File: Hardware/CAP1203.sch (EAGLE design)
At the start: 25 parts, among them J1 Qwiic Right Angle, J2 Qwiic Right Angle, J3 Cap Touch Breakout Pins, J4 I2C Breakout Pins, U1 Cap Touch Slider, U2 CAP1203

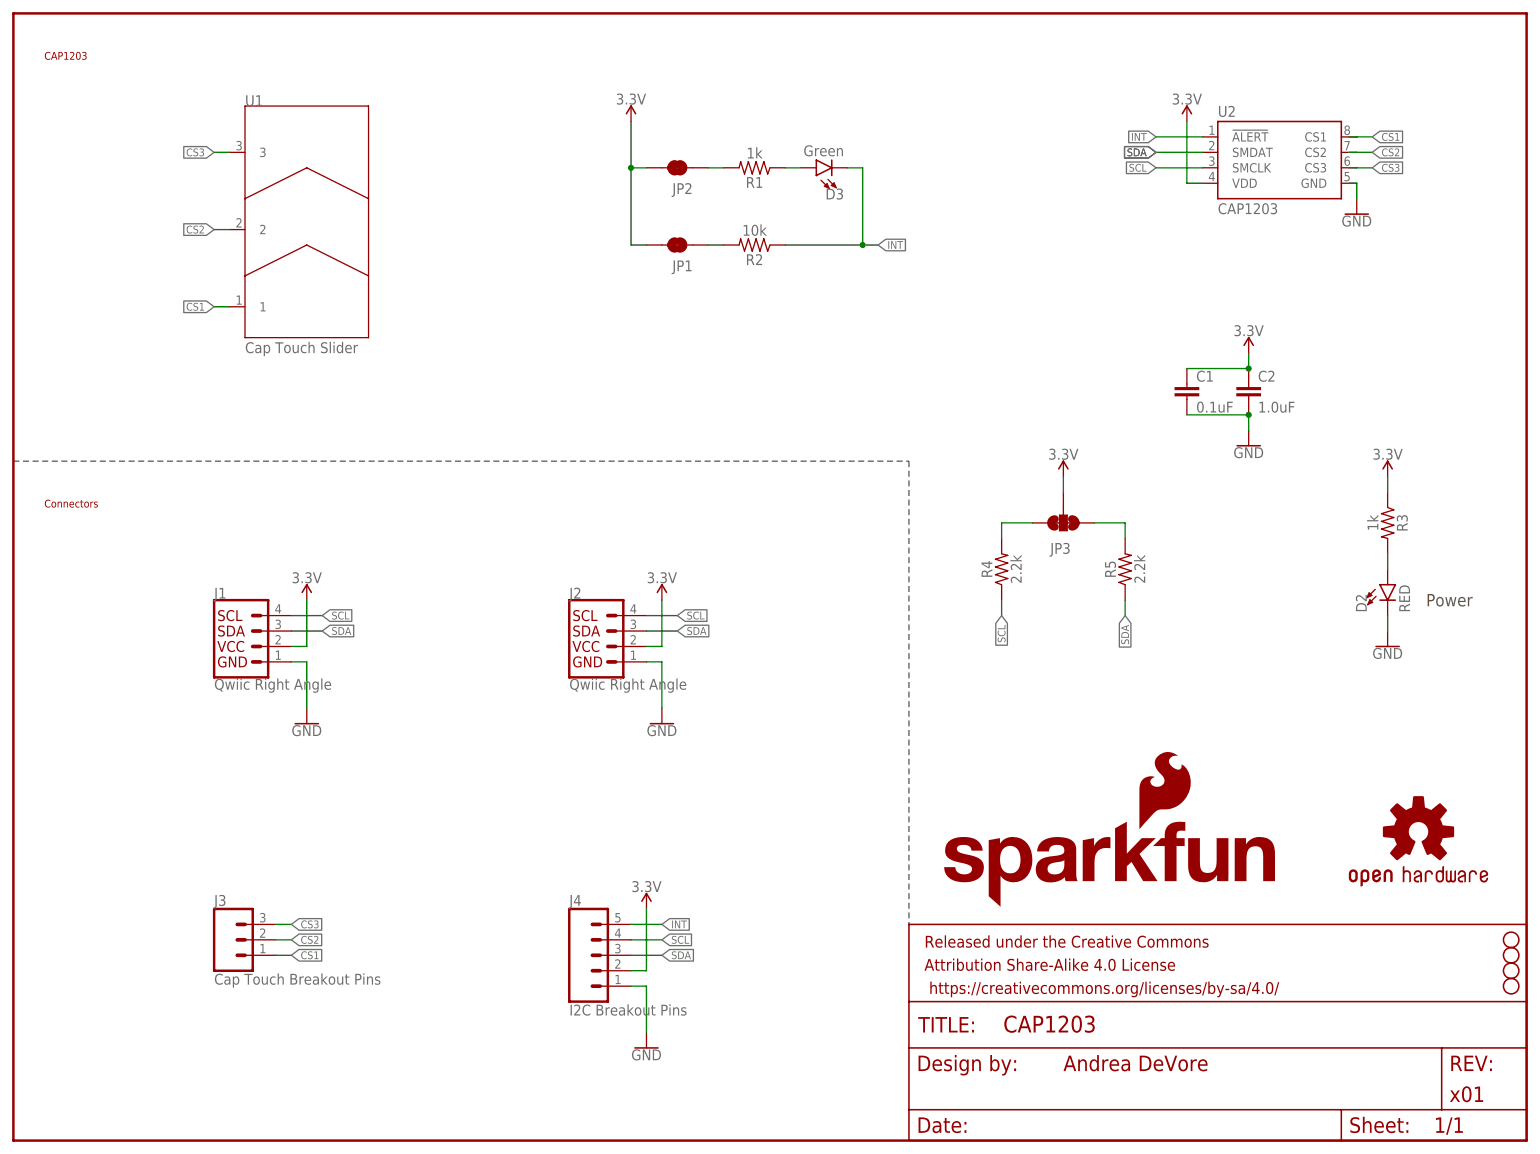
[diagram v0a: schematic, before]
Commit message: Design review revisions
* Updated brd and sch to match SparkFun design standards
* Updated symbol to depict slider
* Updated silkscreen text
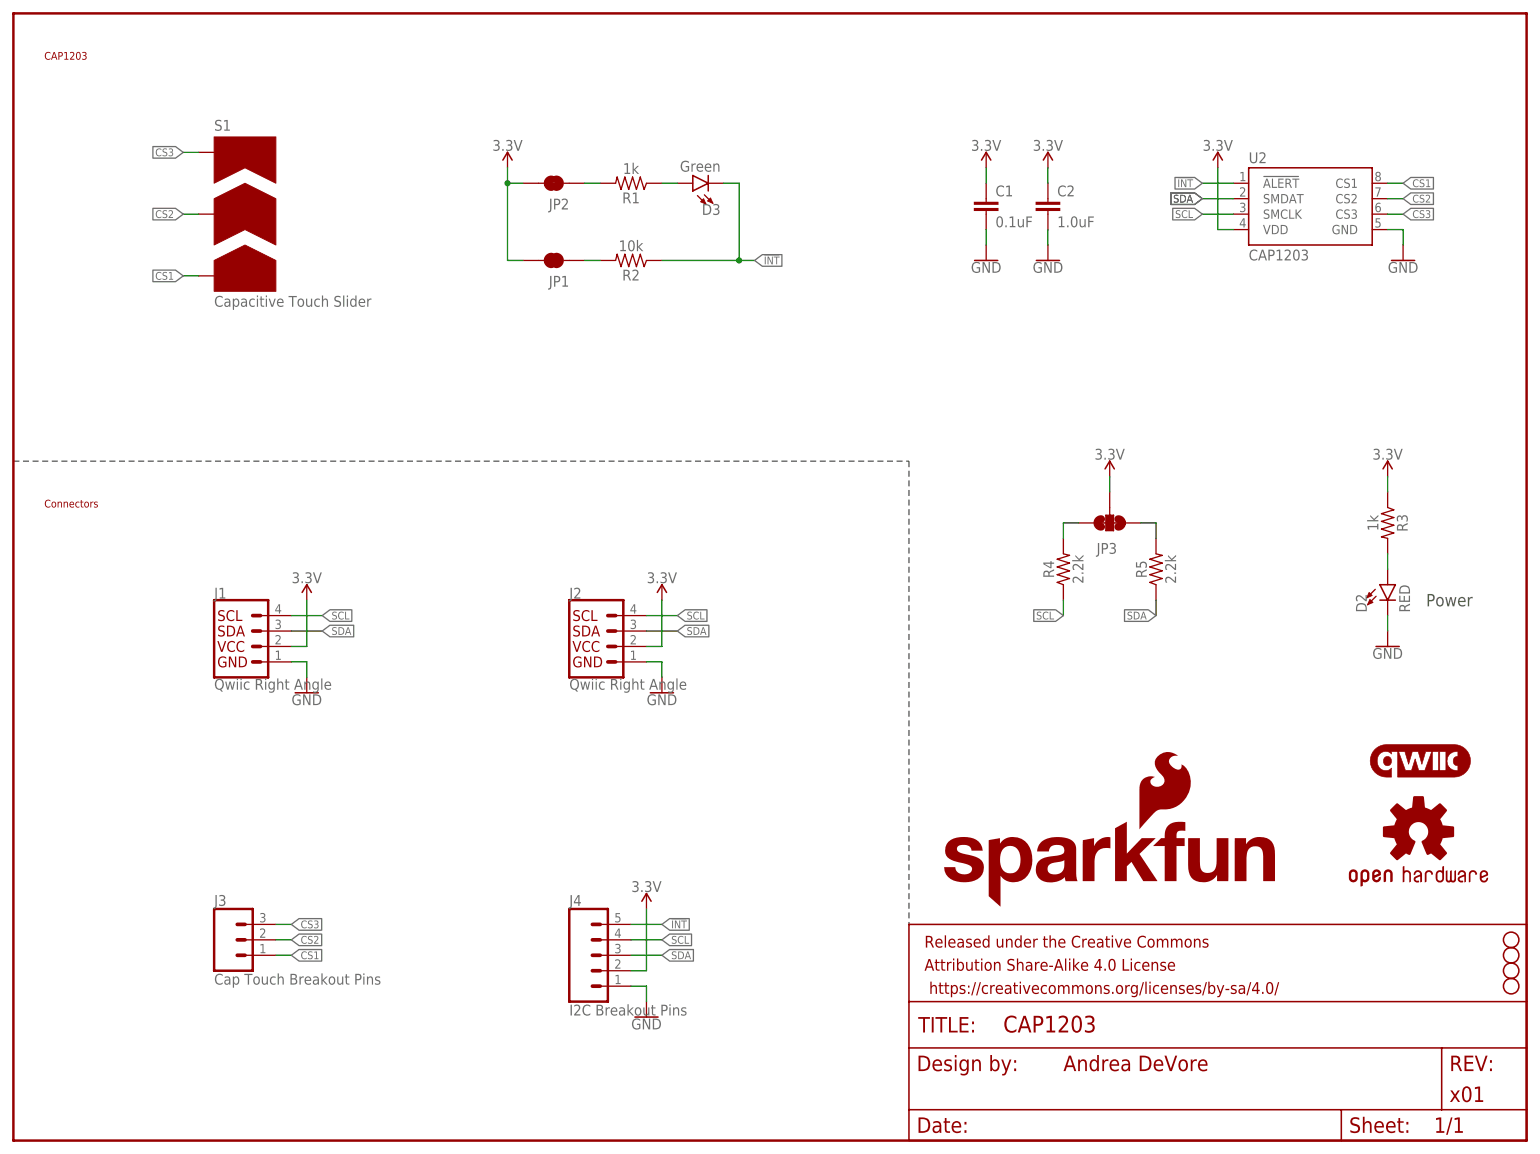
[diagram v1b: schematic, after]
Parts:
- removed U1: Cap Touch Slider, SparkX:CAP_SENSE_SLIDER
- added S1: (no value), SparkX:CAP_SENSE_SLIDER
- added U$17: QWIIC_LOGO_5MM, SparkFun-Aesthetics:QWIIC_LOGO_5MM
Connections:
- net INT renamed !INT
- net CS1: now also S1.1; no longer U1.1
- net CS2: now also S1.2; no longer U1.2
- net CS3: now also S1.3; no longer U1.3
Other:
- note added: "Capacitive Touch Slider"
- moved on the sheet: C1, C2, D3, JP1, JP2, JP3, R1, R2, R4, R5, U2
